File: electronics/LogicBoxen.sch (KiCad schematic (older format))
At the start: 39 parts, among them P1 Input, P2 Output, P3 Power, P4 CONN_01X05, P5 CONN_01X05, P6 CONN_01X06, Q1 Q_NMOS_DGS, SW1 DIPS_04, U1 4015, U2 4050, U3 4015, U4 4050, U6 4051

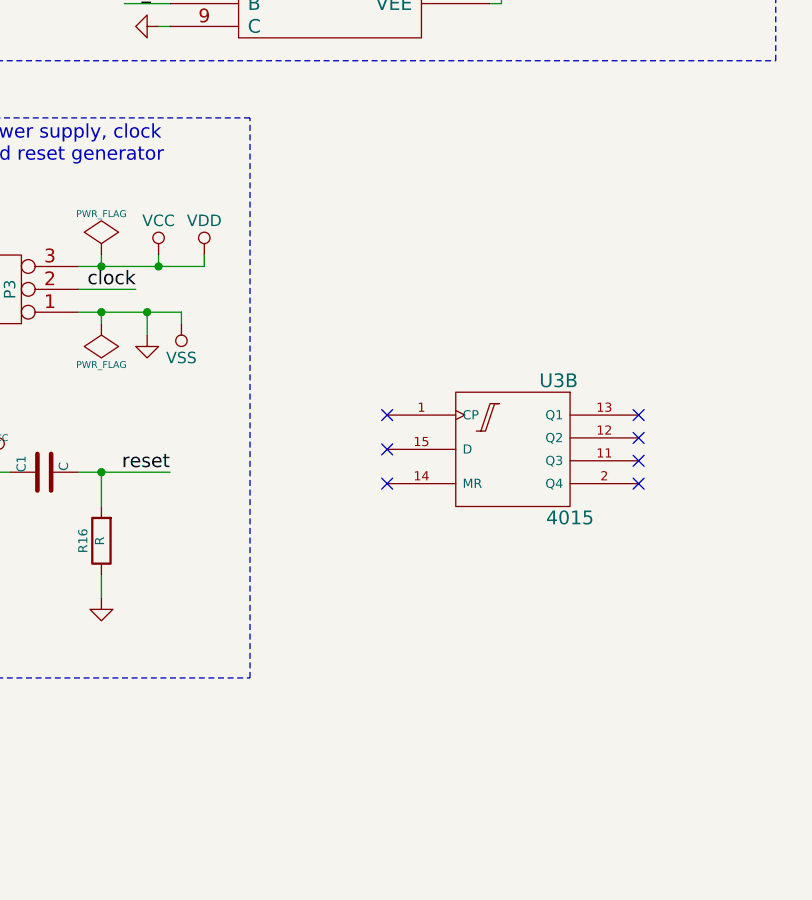
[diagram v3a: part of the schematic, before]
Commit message: Add bypass caps to all ICs
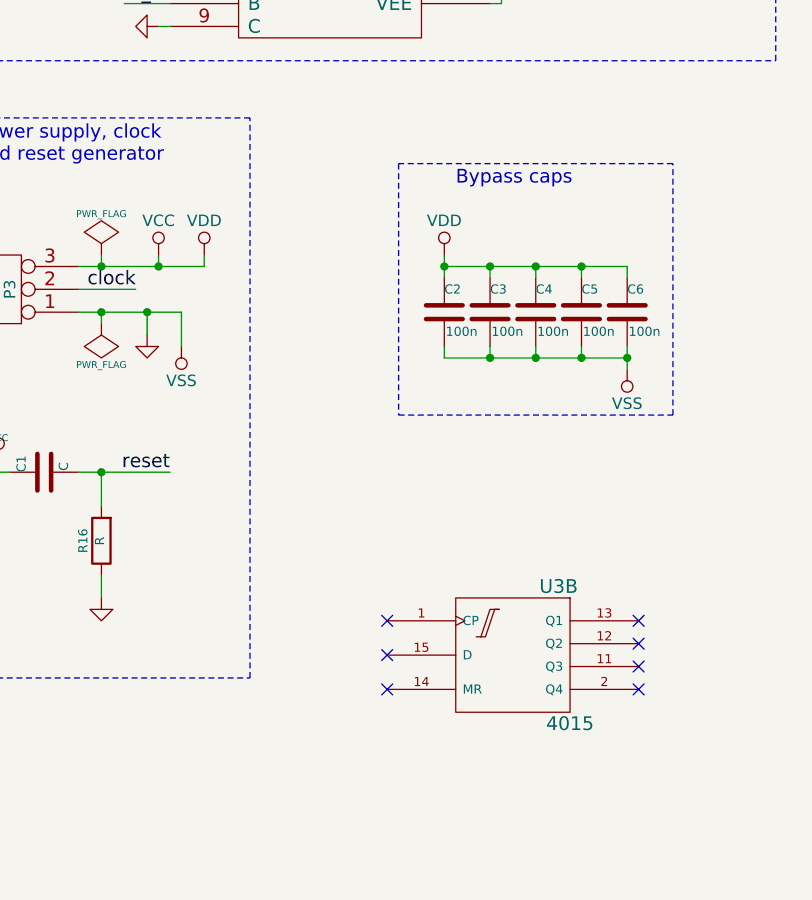
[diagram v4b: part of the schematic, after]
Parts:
- added C2, C3, C4, C5, C6: 100n, Capacitors_SMD:C_0402, symbol C
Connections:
- net GND: now also C2.2, C3.2, C4.2, C5.2, C6.2
- net VCC: now also C2.1, C3.1, C4.1, C5.1, C6.1
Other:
- note added: "Bypass caps"
- moved on the sheet: U3B
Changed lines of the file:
@@
 $EndComp
 $Comp
-L GND-RESCUE-LogicBoxen #PWR01
+L GND-RESCUE-LogicBoxen #PWR10
 U 1 1 555B2EBC
 P 5250 3850
-F 0 "#PWR01" H 5250 3850 30  0001 C CNN
+F 0 "#PWR10" H 5250 3850 30  0001 C CNN
 F 1 "GND" H 5250 3780 30  0001 C CNN
 F 2 "" H 5250 3850 60  0000 C CNN
@@
 $EndComp
 $Comp
-L GND-RESCUE-LogicBoxen #PWR02
+L GND-RESCUE-LogicBoxen #PWR11
 U 1 1 555B3F85
 P 1500 4200
-F 0 "#PWR02" H 1500 4200 30  0001 C CNN
+F 0 "#PWR11" H 1500 4200 30  0001 C CNN
 F 1 "GND" H 1500 4130 30  0001 C CNN
 F 2 "" H 1500 4200 60  0000 C CNN
@@
 $EndComp
 $Comp
-L GND-RESCUE-LogicBoxen #PWR03
+L GND-RESCUE-LogicBoxen #PWR20
 U 1 1 555B7DFC
 P 5150 6350
-F 0 "#PWR03" H 5150 6350 30  0001 C CNN
+F 0 "#PWR20" H 5150 6350 30  0001 C CNN
 F 1 "GND" H 5150 6280 30  0001 C CNN
 F 2 "" H 5150 6350 60  0000 C CNN
@@
 in_b
 $Comp
-L GND-RESCUE-LogicBoxen #PWR04
+L GND-RESCUE-LogicBoxen #PWR6
 U 1 1 555FB14F
 P 1650 2500
-F 0 "#PWR04" H 1650 2500 30  0001 C CNN
+F 0 "#PWR6" H 1650 2500 30  0001 C CNN
 F 1 "GND" H 1650 2430 30  0001 C CNN
 F 2 "" H 1650 2500 60  0000 C CNN
@@
 $EndComp
 $Comp
-L GND-RESCUE-LogicBoxen #PWR05
+L GND-RESCUE-LogicBoxen #PWR3
 U 1 1 5599261E
 P 5250 1900
-F 0 "#PWR05" H 5250 1900 30  0001 C CNN
+F 0 "#PWR3" H 5250 1900 30  0001 C CNN
 F 1 "GND" H 5250 1830 30  0001 C CNN
 F 2 "" H 5250 1900 60  0000 C CNN
@@
 $EndComp
 $Comp
-L VCC #PWR06
+L VCC #PWR8
 U 1 1 559DD663
 P 9750 3200
-F 0 "#PWR06" H 9750 3300 30  0001 C CNN
+F 0 "#PWR8" H 9750 3300 30  0001 C CNN
 F 1 "VCC" H 9750 3300 30  0000 C CNN
 F 2 "" H 9750 3200 60  0000 C CNN
@@
 $EndComp
 $Comp
-L GND #PWR07
+L GND #PWR5
 U 1 1 559DFD6D
 P 7450 2150
-F 0 "#PWR07" H 7450 2150 30  0001 C CNN
+F 0 "#PWR5" H 7450 2150 30  0001 C CNN
 F 1 "GND" H 7450 2080 30  0001 C CNN
 F 2 "" H 7450 2150 60  0000 C CNN
@@
 $EndComp
 $Comp
-L VCC #PWR08
+L VCC #PWR2
 U 1 1 559E03EB
 P 7900 1700
-F 0 "#PWR08" H 7900 1800 30  0001 C CNN
+F 0 "#PWR2" H 7900 1800 30  0001 C CNN
 F 1 "VCC" H 7900 1800 30  0000 C CNN
 F 2 "" H 7900 1700 60  0000 C CNN
@@
 $EndComp
 $Comp
-L GND #PWR09
+L GND #PWR15
 U 1 1 559FB6AF
 P 8200 4700
-F 0 "#PWR09" H 8200 4700 30  0001 C CNN
+F 0 "#PWR15" H 8200 4700 30  0001 C CNN
 F 1 "GND" H 8200 4630 30  0001 C CNN
 F 2 "" H 8200 4700 60  0000 C CNN
@@
 $EndComp
 $Comp
-L PWR_FLAG #FLG010
+L PWR_FLAG #FLG1
 U 1 1 559FBF05
 P 8000 4350
-F 0 "#FLG010" H 8000 4445 30  0001 C CNN
+F 0 "#FLG1" H 8000 4445 30  0001 C CNN
 F 1 "PWR_FLAG" H 8000 4530 30  0000 C CNN
 F 2 "" H 8000 4350 60  0000 C CNN
@@
 $EndComp
 $Comp
-L PWR_FLAG #FLG011
+L PWR_FLAG #FLG2
 U 1 1 559FBF4F
 P 8000 4650
-F 0 "#FLG011" H 8000 4745 30  0001 C CNN
+F 0 "#FLG2" H 8000 4745 30  0001 C CNN
 F 1 "PWR_FLAG" H 8000 4830 30  0000 C CNN
 F 2 "" H 8000 4650 60  0000 C CNN
@@
 $EndComp
 $Comp
-L GND #PWR012
+L GND #PWR19
 U 1 1 559FFD2C
 P 8000 5850
-F 0 "#PWR012" H 8000 5850 30  0001 C CNN
+F 0 "#PWR19" H 8000 5850 30  0001 C CNN
 F 1 "GND" H 8000 5780 30  0001 C CNN
 F 2 "" H 8000 5850 60  0000 C CNN
@@
 $EndComp
 $Comp
-L VCC #PWR013
+L VCC #PWR18
 U 1 1 55A00C35
 P 7550 5250
-F 0 "#PWR013" H 7550 5350 30  0001 C CNN
+F 0 "#PWR18" H 7550 5350 30  0001 C CNN
 F 1 "VCC" H 7550 5350 30  0000 C CNN
 F 2 "" H 7550 5250 60  0000 C CNN
@@
 $EndComp
 $Comp
-L VSS #PWR014
+L VSS #PWR16
 U 1 1 55A43EE6
-P 8350 4650
-F 0 "#PWR014" H 8350 4500 50  0001 C CNN
-F 1 "VSS" H 8350 4800 50  0000 C CNN
-F 2 "" H 8350 4650 60  0000 C CNN
-F 3 "" H 8350 4650 60  0000 C CNN
-	1    8350 4650
+P 8350 4750
+F 0 "#PWR16" H 8350 4600 50  0001 C CNN
+F 1 "VSS" H 8350 4900 50  0000 C CNN
+F 2 "" H 8350 4750 60  0000 C CNN
+F 3 "" H 8350 4750 60  0000 C CNN
+	1    8350 4750
 	-1   0    0    1
 $EndComp
 $Comp
-L VCC #PWR015
+L VCC #PWR12
 U 1 1 55A443FA
 P 8250 4350
-F 0 "#PWR015" H 8250 4200 50  0001 C CNN
+F 0 "#PWR12" H 8250 4200 50  0001 C CNN
 F 1 "VCC" H 8250 4500 50  0000 C CNN
 F 2 "" H 8250 4350 60  0000 C CNN
@@
 $EndComp
 $Comp
-L VCC #PWR016
+L VCC #PWR4
 U 1 1 55A44F55
 P 10350 1900
-F 0 "#PWR016" H 10350 1750 50  0001 C CNN
+F 0 "#PWR4" H 10350 1750 50  0001 C CNN
 F 1 "VCC" H 10350 2050 50  0000 C CNN
 F 2 "" H 10350 1900 60  0000 C CNN
@@
 $EndComp
 $Comp
-L VDD #PWR017
+L VDD #PWR13
 U 1 1 55A45774
 P 8450 4350
-F 0 "#PWR017" H 8450 4200 50  0001 C CNN
+F 0 "#PWR13" H 8450 4200 50  0001 C CNN
 F 1 "VDD" H 8450 4500 50  0000 C CNN
 F 2 "" H 8450 4350 60  0000 C CNN
@@
 L 4015 U3
 U 2 1 55A43770
-P 9800 5200
-F 0 "U3" H 10000 5500 60  0000 C CNN
-F 1 "4015" H 10050 4900 60  0000 C CNN
-F 2 "Housings_SSOP:TSSOP-16_4.4x5mm_Pitch0.65mm" H 9800 5200 60  0001 C CNN
-F 3 "" H 9800 5200 60  0000 C CNN
-	2    9800 5200
-	1    0    0    -1
-$EndComp
-NoConn ~ 9250 5050
-NoConn ~ 9250 5200
-NoConn ~ 9250 5350
-NoConn ~ 10350 5350
-NoConn ~ 10350 5250
-NoConn ~ 10350 5150
-NoConn ~ 10350 5050
-$Comp
-L GND #PWR018
+P 9800 6100
+F 0 "U3" H 10000 6400 60  0000 C CNN
+F 1 "4015" H 10050 5800 60  0000 C CNN
+F 2 "Housings_SSOP:TSSOP-16_4.4x5mm_Pitch0.65mm" H 9800 6100 60  0001 C CNN
+F 3 "" H 9800 6100 60  0000 C CNN
+	2    9800 6100
+	1    0    0    -1
+$EndComp
+NoConn ~ 9250 5950
+NoConn ~ 9250 6100
+NoConn ~ 9250 6250
+NoConn ~ 10350 6250
+NoConn ~ 10350 6150
+NoConn ~ 10350 6050
+NoConn ~ 10350 5950
+$Comp
+L GND #PWR7
 U 1 1 559DE455
 P 8050 3050
-F 0 "#PWR018" H 8050 3050 30  0001 C CNN
+F 0 "#PWR7" H 8050 3050 30  0001 C CNN
 F 1 "GND" H 8050 2980 30  0001 C CNN
 F 2 "" H 8050 3050 60  0000 C CNN
@@
 	8100 3250 8300 3250
 Wire Wire Line
-	9700 3250 9750 3250
-Wire Wire Line
-	9750 3250 9750 3200
-Wire Wire Line
 	8250 3350 8300 3350
 Wire Wire Line
@@
 Connection ~ 8250 3050
 Wire Wire Line
-	8350 4600 8350 4650
+	8350 4600 8350 4750
 Connection ~ 8200 4600
 Wire Wire Line
@@
 Connection ~ 6400 1550
 $Comp
-L VCC #PWR019
+L VCC #PWR1
 U 1 1 55E4B7FF
 P 6400 1250
-F 0 "#PWR019" H 6400 1350 30  0001 C CNN
+F 0 "#PWR1" H 6400 1350 30  0001 C CNN
 F 1 "VCC" H 6400 1350 30  0000 C CNN
 F 2 "" H 6400 1250 60  0000 C CNN
@@
 	7200 1950 7200 1650
 $Comp
-L GND #PWR020
+L GND #PWR9
 U 1 1 559DDF9D
 P 8250 3350
-F 0 "#PWR020" H 8250 3350 30  0001 C CNN
+F 0 "#PWR9" H 8250 3350 30  0001 C CNN
 F 1 "GND" H 8250 3280 30  0001 C CNN
 F 2 "" H 8250 3350 60  0000 C CNN
@@
 	0    1    1    0
 $EndComp
+Wire Wire Line
+	9700 3250 9750 3250
+Wire Wire Line
+	9750 3250 9750 3200
+$Comp
+L VDD #PWR14
+U 1 1 55F0E374
+P 9500 4350
+F 0 "#PWR14" H 9500 4200 50  0001 C CNN
+F 1 "VDD" H 9500 4500 50  0000 C CNN
+F 2 "" H 9500 4350 60  0000 C CNN
+F 3 "" H 9500 4350 60  0000 C CNN
+	1    9500 4350
+	1    0    0    -1
+$EndComp
+$Comp
+L C C2
+U 1 1 55F0E6FE
+P 9500 4600
+F 0 "C2" H 9500 4700 40  0000 L CNN
+F 1 "100n" H 9506 4515 40  0000 L CNN
+F 2 "Capacitors_SMD:C_0402" H 9538 4450 30  0001 C CNN
+F 3 "" H 9500 4600 60  0000 C CNN
+	1    9500 4600
+	1    0    0    -1
+$EndComp
+$Comp
+L C C3
+U 1 1 55F0E8BF
+P 9700 4600
+F 0 "C3" H 9700 4700 40  0000 L CNN
+F 1 "100n" H 9706 4515 40  0000 L CNN
+F 2 "Capacitors_SMD:C_0402" H 9738 4450 30  0001 C CNN
+F 3 "" H 9700 4600 60  0000 C CNN
+	1    9700 4600
+	1    0    0    -1
+$EndComp
+$Comp
+L C C4
+U 1 1 55F0E96E
+P 9900 4600
+F 0 "C4" H 9900 4700 40  0000 L CNN
+F 1 "100n" H 9906 4515 40  0000 L CNN
+F 2 "Capacitors_SMD:C_0402" H 9938 4450 30  0001 C CNN
+F 3 "" H 9900 4600 60  0000 C CNN
+	1    9900 4600
+	1    0    0    -1
+$EndComp
+$Comp
+L C C5
+U 1 1 55F0EA20
+P 10100 4600
+F 0 "C5" H 10100 4700 40  0000 L CNN
+F 1 "100n" H 10106 4515 40  0000 L CNN
+F 2 "Capacitors_SMD:C_0402" H 10138 4450 30  0001 C CNN
+F 3 "" H 10100 4600 60  0000 C CNN
+	1    10100 4600
+	1    0    0    -1
+$EndComp
+Wire Wire Line
+	9500 4350 9500 4450
+Wire Wire Line
+	9700 4450 9700 4400
+Wire Wire Line
+	9500 4400 10300 4400
+Connection ~ 9500 4400
+Wire Wire Line
+	9900 4400 9900 4450
+Connection ~ 9700 4400
+Wire Wire Line
+	10100 4400 10100 4450
+Connection ~ 9900 4400
+Wire Wire Line
+	9900 4800 9900 4750
+Wire Wire Line
+	9500 4800 10300 4800
+Connection ~ 10100 4800
+Wire Wire Line
+	9700 4750 9700 4800
+Connection ~ 9900 4800
+Wire Wire Line
+	9500 4750 9500 4800
+Connection ~ 9700 4800
+Wire Notes Line
+	9300 3950 9300 5050
+Wire Notes Line
+	9300 5050 10500 5050
+Text Notes 9550 4050 0    60   ~ 0
+Bypass caps
+$Comp
+L VSS #PWR17
+U 1 1 55F12929
+P 10300 4850
+F 0 "#PWR17" H 10300 4700 50  0001 C CNN
+F 1 "VSS" H 10300 5000 50  0000 C CNN
+F 2 "" H 10300 4850 60  0000 C CNN
+F 3 "" H 10300 4850 60  0000 C CNN
+	1    10300 4850
+	-1   0    0    1
+$EndComp
+$Comp
+L C C6
+U 1 1 55F12E9C
+P 10300 4600
+F 0 "C6" H 10300 4700 40  0000 L CNN
+F 1 "100n" H 10306 4515 40  0000 L CNN
+F 2 "Capacitors_SMD:C_0402" H 10338 4450 30  0001 C CNN
+F 3 "" H 10300 4600 60  0000 C CNN
+	1    10300 4600
+	1    0    0    -1
+$EndComp
+Wire Notes Line
+	10500 5050 10500 3950
+Wire Notes Line
+	10500 3950 9300 3950
+Wire Wire Line
+	10300 4400 10300 4450
+Connection ~ 10100 4400
+Wire Wire Line
+	10300 4750 10300 4850
+Wire Wire Line
+	10100 4750 10100 4800
+Connection ~ 10300 4800
 $EndSCHEMATC

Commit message: Fix bug in schematic
Vede has to be connected to ground, of course -.-
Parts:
- C1: value C -> 100n
- Q1: symbol Q_NMOS_DGS -> Q_NMOS_DGS-RESCUE-LogicBoxen
- R16: value R -> 10k
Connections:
- net GND: now also U6.7 (VEE)
- net VCC: no longer U6.7 (VEE)
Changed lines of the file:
@@
 $EndComp
 $Comp
-L GND-RESCUE-LogicBoxen #PWR10
+L GND-RESCUE-LogicBoxen #PWR01
 U 1 1 555B2EBC
 P 5250 3850
-F 0 "#PWR10" H 5250 3850 30  0001 C CNN
+F 0 "#PWR01" H 5250 3850 30  0001 C CNN
 F 1 "GND" H 5250 3780 30  0001 C CNN
 F 2 "" H 5250 3850 60  0000 C CNN
@@
 $EndComp
 $Comp
-L GND-RESCUE-LogicBoxen #PWR11
+L GND-RESCUE-LogicBoxen #PWR02
 U 1 1 555B3F85
 P 1500 4200
-F 0 "#PWR11" H 1500 4200 30  0001 C CNN
+F 0 "#PWR02" H 1500 4200 30  0001 C CNN
 F 1 "GND" H 1500 4130 30  0001 C CNN
 F 2 "" H 1500 4200 60  0000 C CNN
@@
 $EndComp
 $Comp
-L GND-RESCUE-LogicBoxen #PWR20
+L GND-RESCUE-LogicBoxen #PWR03
 U 1 1 555B7DFC
 P 5150 6350
-F 0 "#PWR20" H 5150 6350 30  0001 C CNN
+F 0 "#PWR03" H 5150 6350 30  0001 C CNN
 F 1 "GND" H 5150 6280 30  0001 C CNN
 F 2 "" H 5150 6350 60  0000 C CNN
@@
 in_b
 $Comp
-L GND-RESCUE-LogicBoxen #PWR6
+L GND-RESCUE-LogicBoxen #PWR04
 U 1 1 555FB14F
 P 1650 2500
-F 0 "#PWR6" H 1650 2500 30  0001 C CNN
+F 0 "#PWR04" H 1650 2500 30  0001 C CNN
 F 1 "GND" H 1650 2430 30  0001 C CNN
 F 2 "" H 1650 2500 60  0000 C CNN
@@
 $EndComp
 $Comp
-L GND-RESCUE-LogicBoxen #PWR3
+L GND-RESCUE-LogicBoxen #PWR05
 U 1 1 5599261E
 P 5250 1900
-F 0 "#PWR3" H 5250 1900 30  0001 C CNN
+F 0 "#PWR05" H 5250 1900 30  0001 C CNN
 F 1 "GND" H 5250 1830 30  0001 C CNN
 F 2 "" H 5250 1900 60  0000 C CNN
@@
 $EndComp
 $Comp
-L VCC #PWR8
-U 1 1 559DD663
-P 9750 3200
-F 0 "#PWR8" H 9750 3300 30  0001 C CNN
-F 1 "VCC" H 9750 3300 30  0000 C CNN
-F 2 "" H 9750 3200 60  0000 C CNN
-F 3 "" H 9750 3200 60  0000 C CNN
-	1    9750 3200
-	1    0    0    -1
-$EndComp
-$Comp
 L DIPS_04 SW1
 U 1 1 559DF1D9
@@
 $EndComp
 $Comp
-L GND #PWR5
+L GND #PWR06
 U 1 1 559DFD6D
 P 7450 2150
-F 0 "#PWR5" H 7450 2150 30  0001 C CNN
+F 0 "#PWR06" H 7450 2150 30  0001 C CNN
 F 1 "GND" H 7450 2080 30  0001 C CNN
 F 2 "" H 7450 2150 60  0000 C CNN
@@
 $EndComp
 $Comp
-L VCC #PWR2
+L VCC #PWR07
 U 1 1 559E03EB
 P 7900 1700
-F 0 "#PWR2" H 7900 1800 30  0001 C CNN
+F 0 "#PWR07" H 7900 1800 30  0001 C CNN
 F 1 "VCC" H 7900 1800 30  0000 C CNN
 F 2 "" H 7900 1700 60  0000 C CNN
@@
 $EndComp
 $Comp
-L GND #PWR15
+L GND #PWR08
 U 1 1 559FB6AF
 P 8200 4700
-F 0 "#PWR15" H 8200 4700 30  0001 C CNN
+F 0 "#PWR08" H 8200 4700 30  0001 C CNN
 F 1 "GND" H 8200 4630 30  0001 C CNN
 F 2 "" H 8200 4700 60  0000 C CNN
@@
 $EndComp
 $Comp
-L PWR_FLAG #FLG1
+L PWR_FLAG #FLG09
 U 1 1 559FBF05
 P 8000 4350
-F 0 "#FLG1" H 8000 4445 30  0001 C CNN
+F 0 "#FLG09" H 8000 4445 30  0001 C CNN
 F 1 "PWR_FLAG" H 8000 4530 30  0000 C CNN
 F 2 "" H 8000 4350 60  0000 C CNN
@@
 $EndComp
 $Comp
-L PWR_FLAG #FLG2
+L PWR_FLAG #FLG010
 U 1 1 559FBF4F
 P 8000 4650
-F 0 "#FLG2" H 8000 4745 30  0001 C CNN
+F 0 "#FLG010" H 8000 4745 30  0001 C CNN
 F 1 "PWR_FLAG" H 8000 4830 30  0000 C CNN
 F 2 "" H 8000 4650 60  0000 C CNN
@@
 P 8000 5600
 F 0 "R16" V 8080 5600 40  0000 C CNN
-F 1 "R" V 8007 5601 40  0000 C CNN
+F 1 "10k" V 8007 5601 40  0000 C CNN
 F 2 "Resistors_SMD:R_0402" V 7930 5600 30  0001 C CNN
 F 3 "" H 8000 5600 30  0000 C CNN
@@
 P 7750 5300
 F 0 "C1" H 7750 5400 40  0000 L CNN
-F 1 "C" H 7756 5215 40  0000 L CNN
+F 1 "100n" H 7756 5215 40  0000 L CNN
 F 2 "Capacitors_SMD:C_0402" H 7788 5150 30  0001 C CNN
 F 3 "" H 7750 5300 60  0000 C CNN
@@
 $EndComp
 $Comp
-L GND #PWR19
+L GND #PWR011
 U 1 1 559FFD2C
 P 8000 5850
-F 0 "#PWR19" H 8000 5850 30  0001 C CNN
+F 0 "#PWR011" H 8000 5850 30  0001 C CNN
 F 1 "GND" H 8000 5780 30  0001 C CNN
 F 2 "" H 8000 5850 60  0000 C CNN
@@
 $EndComp
 $Comp
-L VCC #PWR18
+L VCC #PWR012
 U 1 1 55A00C35
 P 7550 5250
-F 0 "#PWR18" H 7550 5350 30  0001 C CNN
+F 0 "#PWR012" H 7550 5350 30  0001 C CNN
 F 1 "VCC" H 7550 5350 30  0000 C CNN
 F 2 "" H 7550 5250 60  0000 C CNN
@@
 $EndComp
 $Comp
-L VSS #PWR16
+L VSS #PWR013
 U 1 1 55A43EE6
 P 8350 4750
-F 0 "#PWR16" H 8350 4600 50  0001 C CNN
+F 0 "#PWR013" H 8350 4600 50  0001 C CNN
 F 1 "VSS" H 8350 4900 50  0000 C CNN
 F 2 "" H 8350 4750 60  0000 C CNN
@@
 $EndComp
 $Comp
-L VCC #PWR12
+L VCC #PWR014
 U 1 1 55A443FA
 P 8250 4350
-F 0 "#PWR12" H 8250 4200 50  0001 C CNN
+F 0 "#PWR014" H 8250 4200 50  0001 C CNN
 F 1 "VCC" H 8250 4500 50  0000 C CNN
 F 2 "" H 8250 4350 60  0000 C CNN
@@
 $EndComp
 $Comp
-L VCC #PWR4
+L VCC #PWR015
 U 1 1 55A44F55
 P 10350 1900
-F 0 "#PWR4" H 10350 1750 50  0001 C CNN
+F 0 "#PWR015" H 10350 1750 50  0001 C CNN
 F 1 "VCC" H 10350 2050 50  0000 C CNN
 F 2 "" H 10350 1900 60  0000 C CNN
@@
 $EndComp
 $Comp
-L VDD #PWR13
+L VDD #PWR016
 U 1 1 55A45774
 P 8450 4350
-F 0 "#PWR13" H 8450 4200 50  0001 C CNN
+F 0 "#PWR016" H 8450 4200 50  0001 C CNN
 F 1 "VDD" H 8450 4500 50  0000 C CNN
 F 2 "" H 8450 4350 60  0000 C CNN
@@
 NoConn ~ 10350 5950
 $Comp
-L GND #PWR7
+L GND #PWR017
 U 1 1 559DE455
 P 8050 3050
-F 0 "#PWR7" H 8050 3050 30  0001 C CNN
+F 0 "#PWR017" H 8050 3050 30  0001 C CNN
 F 1 "GND" H 8050 2980 30  0001 C CNN
 F 2 "" H 8050 3050 60  0000 C CNN
@@
 led_main
 $Comp
-L Q_NMOS_DGS Q1
+L Q_NMOS_DGS-RESCUE-LogicBoxen Q1
 U 1 1 55DE3494
 P 10250 2150
@@
 Connection ~ 6400 1550
 $Comp
-L VCC #PWR1
+L VCC #PWR018
 U 1 1 55E4B7FF
 P 6400 1250
-F 0 "#PWR1" H 6400 1350 30  0001 C CNN
+F 0 "#PWR018" H 6400 1350 30  0001 C CNN
 F 1 "VCC" H 6400 1350 30  0000 C CNN
 F 2 "" H 6400 1250 60  0000 C CNN
@@
 	7200 1950 7200 1650
 $Comp
-L GND #PWR9
+L GND #PWR019
 U 1 1 559DDF9D
 P 8250 3350
-F 0 "#PWR9" H 8250 3350 30  0001 C CNN
+F 0 "#PWR019" H 8250 3350 30  0001 C CNN
 F 1 "GND" H 8250 3280 30  0001 C CNN
 F 2 "" H 8250 3350 60  0000 C CNN
@@
 	0    1    1    0
 $EndComp
-Wire Wire Line
-	9700 3250 9750 3250
-Wire Wire Line
-	9750 3250 9750 3200
-$Comp
-L VDD #PWR14
+$Comp
+L VDD #PWR020
 U 1 1 55F0E374
 P 9500 4350
-F 0 "#PWR14" H 9500 4200 50  0001 C CNN
+F 0 "#PWR020" H 9500 4200 50  0001 C CNN
 F 1 "VDD" H 9500 4500 50  0000 C CNN
 F 2 "" H 9500 4350 60  0000 C CNN
@@
 Bypass caps
 $Comp
-L VSS #PWR17
+L VSS #PWR021
 U 1 1 55F12929
 P 10300 4850
-F 0 "#PWR17" H 10300 4700 50  0001 C CNN
+F 0 "#PWR021" H 10300 4700 50  0001 C CNN
 F 1 "VSS" H 10300 5000 50  0000 C CNN
 F 2 "" H 10300 4850 60  0000 C CNN
@@
 	10100 4750 10100 4800
 Connection ~ 10300 4800
+$Comp
+L GND #PWR022
+U 1 1 56661D49
+P 9750 3300
+F 0 "#PWR022" H 9750 3050 50  0001 C CNN
+F 1 "GND" H 9750 3150 50  0000 C CNN
+F 2 "" H 9750 3300 50  0000 C CNN
+F 3 "" H 9750 3300 50  0000 C CNN
+	1    9750 3300
+	1    0    0    -1
+$EndComp
+Wire Wire Line
+	9750 3300 9750 3250
+Wire Wire Line
+	9750 3250 9700 3250
 $EndSCHEMATC
